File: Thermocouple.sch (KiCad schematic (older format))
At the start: 22 parts, among them P2 CONN_2, P3 CONN_3X2, U10 LMT84, U11 OPA4170, U9 MCP3901

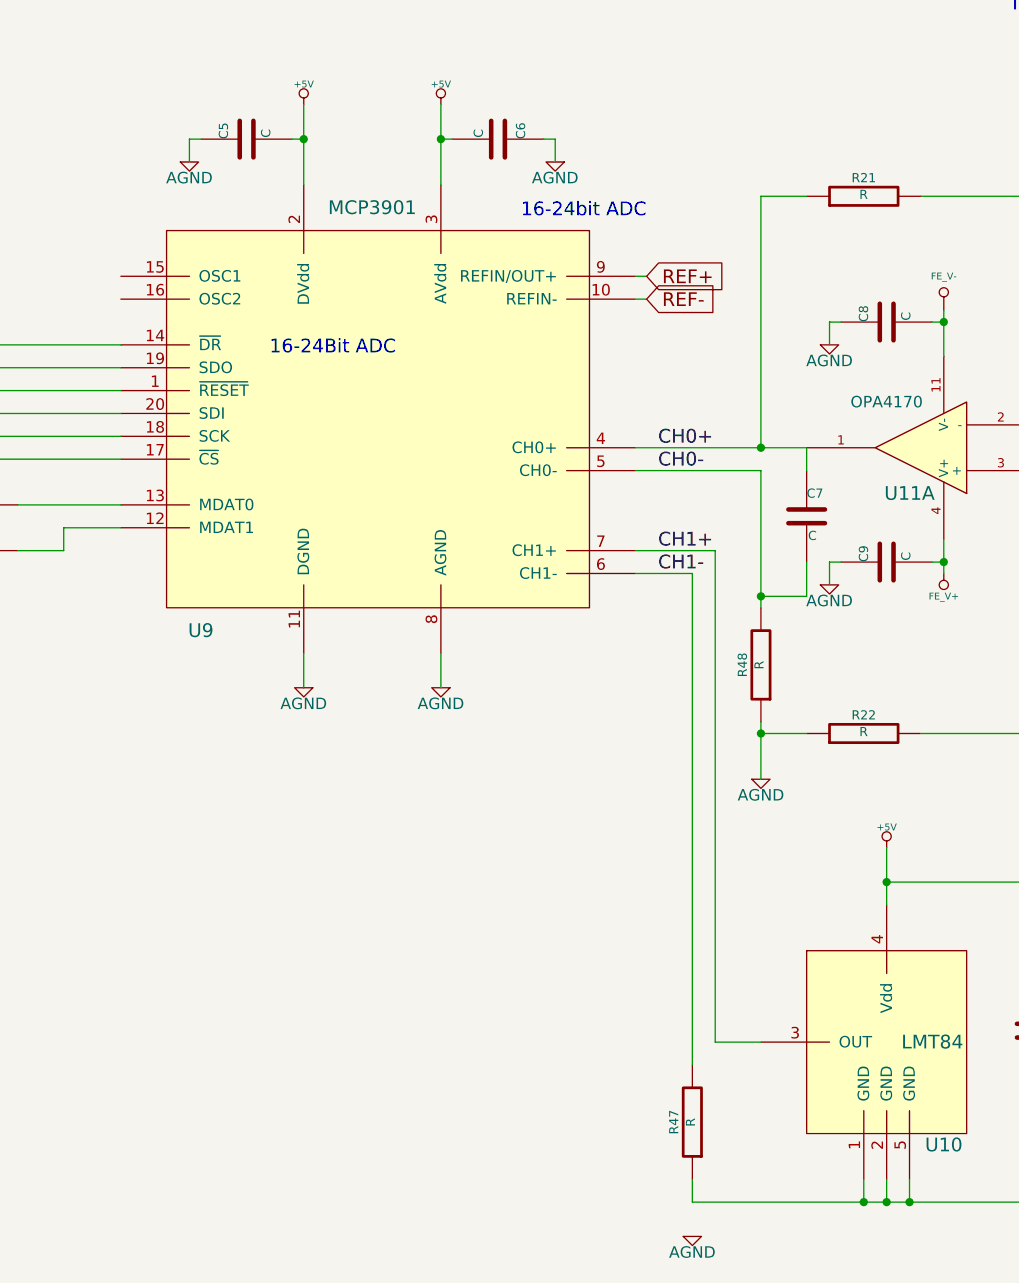
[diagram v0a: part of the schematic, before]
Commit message: Updates from Layout Work Session 4 video
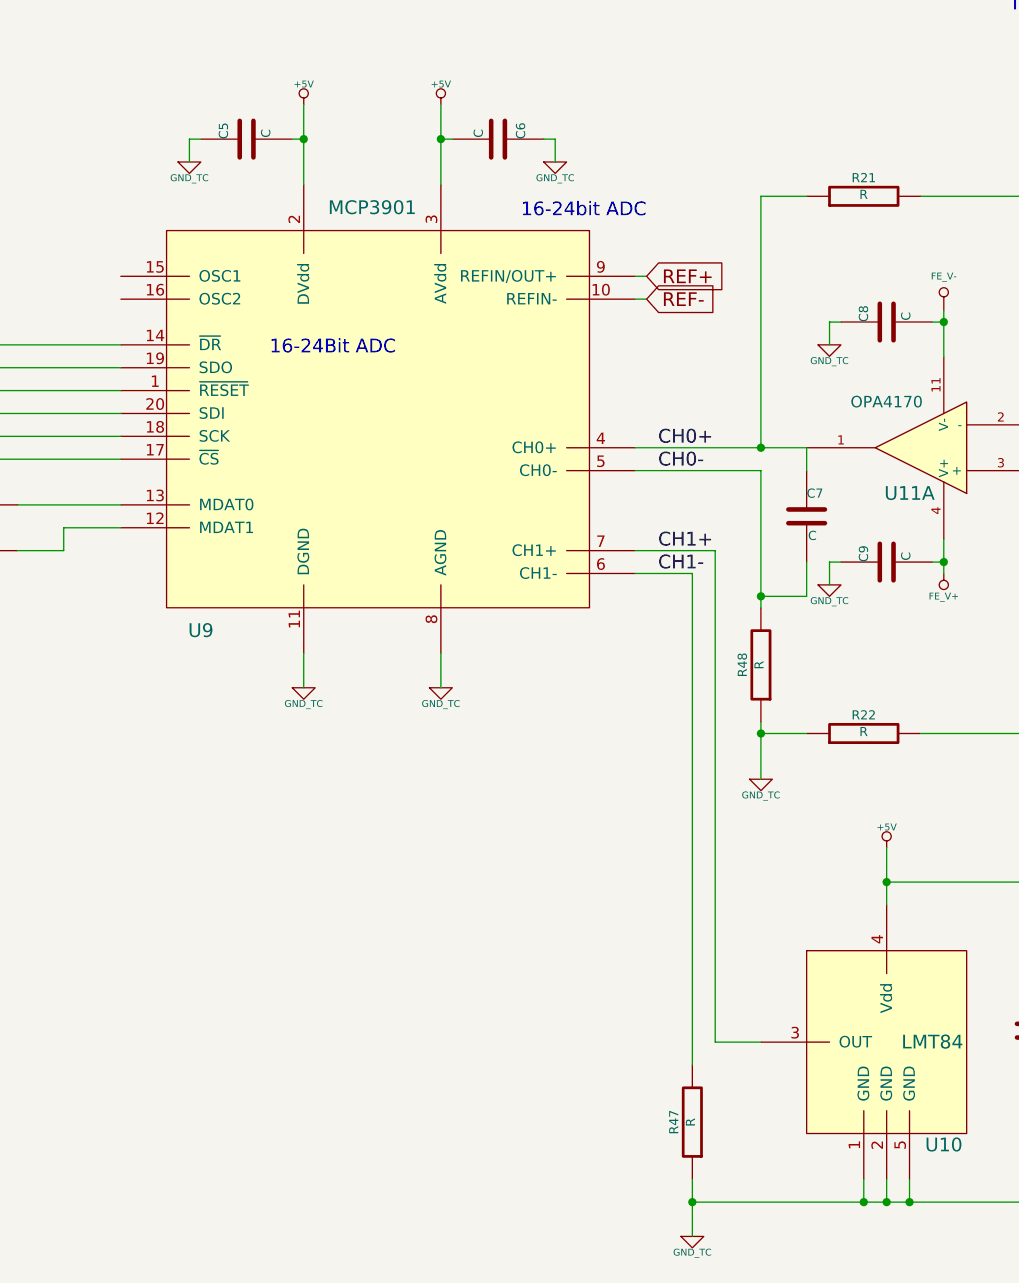
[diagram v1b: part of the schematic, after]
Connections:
- net AGND is gone; now on net GND_TC: C5.1, C6.1, C8.1, C9.1, R22.1, R48.1, U9.11 (DGND), U9.8 (AGND)
- net GND_TC: now reaches C10.2, R47.1, U10.1 (GND), U10.2 (GND), U10.5 (GND)
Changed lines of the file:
@@
 	0    -1   -1   0
-$EndComp
-$Comp
-L AGND #PWR046
-U 1 1 52F01EB3
-P 4500 4450
-F 0 "#PWR046" H 4500 4450 40  0001 C CNN
-F 1 "AGND" H 4500 4380 50  0000 C CNN
-F 2 "" H 4500 4450 60  0000 C CNN
-F 3 "" H 4500 4450 60  0000 C CNN
-	1    4500 4450
-	1    0    0    -1
 $EndComp
 Text Notes 8600 2100 0    60   ~ 0
@@
 $EndComp
 $Comp
-L AGND #PWR047
-U 1 1 53054233
-P 4200 6450
-F 0 "#PWR047" H 4200 6450 40  0001 C CNN
-F 1 "AGND" H 4200 6380 50  0000 C CNN
-F 2 "" H 4200 6450 60  0000 C CNN
-F 3 "" H 4200 6450 60  0000 C CNN
-	1    4200 6450
-	1    0    0    -1
-$EndComp
-$Comp
-L +5V #PWR048
+L +5V #PWR041
 U 1 1 530546E7
 P 5050 4750
-F 0 "#PWR048" H 5050 4840 20  0001 C CNN
+F 0 "#PWR041" H 5050 4840 20  0001 C CNN
 F 1 "+5V" H 5050 4840 30  0000 C CNN
 F 2 "" H 5050 4750 60  0000 C CNN
@@
 $EndComp
 $Comp
-L AGND #PWR049
-U 1 1 530549E4
-P 4800 2550
-F 0 "#PWR049" H 4800 2550 40  0001 C CNN
-F 1 "AGND" H 4800 2480 50  0000 C CNN
-F 2 "" H 4800 2550 60  0000 C CNN
-F 3 "" H 4800 2550 60  0000 C CNN
-	1    4800 2550
-	1    0    0    -1
-$EndComp
-$Comp
 L C C9
 U 1 1 53054A99
@@
 $EndComp
 $Comp
-L AGND #PWR050
-U 1 1 53054AA0
-P 4800 3600
-F 0 "#PWR050" H 4800 3600 40  0001 C CNN
-F 1 "AGND" H 4800 3530 50  0000 C CNN
-F 2 "" H 4800 3600 60  0000 C CNN
-F 3 "" H 4800 3600 60  0000 C CNN
-	1    4800 3600
-	1    0    0    -1
-$EndComp
-$Comp
-L +5V #PWR051
+L +5V #PWR042
 U 1 1 53054B2C
 P 3100 1500
-F 0 "#PWR051" H 3100 1590 20  0001 C CNN
+F 0 "#PWR042" H 3100 1590 20  0001 C CNN
 F 1 "+5V" H 3100 1590 30  0000 C CNN
 F 2 "" H 3100 1500 60  0000 C CNN
@@
 $EndComp
 $Comp
-L AGND #PWR052
-U 1 1 53054C58
-P 3600 1750
-F 0 "#PWR052" H 3600 1750 40  0001 C CNN
-F 1 "AGND" H 3600 1680 50  0000 C CNN
-F 2 "" H 3600 1750 60  0000 C CNN
-F 3 "" H 3600 1750 60  0000 C CNN
-	1    3600 1750
-	-1   0    0    -1
-$EndComp
-$Comp
-L AGND #PWR053
-U 1 1 5305505B
-P 3100 4050
-F 0 "#PWR053" H 3100 4050 40  0001 C CNN
-F 1 "AGND" H 3100 3980 50  0000 C CNN
-F 2 "" H 3100 4050 60  0000 C CNN
-F 3 "" H 3100 4050 60  0000 C CNN
-	1    3100 4050
-	-1   0    0    -1
-$EndComp
-$Comp
-L AGND #PWR054
-U 1 1 5305533E
-P 2500 4050
-F 0 "#PWR054" H 2500 4050 40  0001 C CNN
-F 1 "AGND" H 2500 3980 50  0000 C CNN
-F 2 "" H 2500 4050 60  0000 C CNN
-F 3 "" H 2500 4050 60  0000 C CNN
-	1    2500 4050
-	-1   0    0    -1
-$EndComp
-$Comp
-L +5V #PWR055
+L +5V #PWR043
 U 1 1 53055345
 P 2500 1500
-F 0 "#PWR055" H 2500 1590 20  0001 C CNN
+F 0 "#PWR043" H 2500 1590 20  0001 C CNN
 F 1 "+5V" H 2500 1590 30  0000 C CNN
 F 2 "" H 2500 1500 60  0000 C CNN
@@
 	0    -1   -1   0
 $EndComp
-$Comp
-L AGND #PWR056
-U 1 1 53055353
-P 2000 1750
-F 0 "#PWR056" H 2000 1750 40  0001 C CNN
-F 1 "AGND" H 2000 1680 50  0000 C CNN
-F 2 "" H 2000 1750 60  0000 C CNN
-F 3 "" H 2000 1750 60  0000 C CNN
-	1    2000 1750
-	1    0    0    -1
-$EndComp
 Text Notes 5900 5550 0    60   ~ 0
 Temperature Sensor
@@
 	4200 3550 4200 5700
 Wire Wire Line
-	4200 6300 4200 6200
+	4200 6200 4200 6450
 Connection ~ 5900 4250
 Wire Wire Line
@@
 	1050 3050 1700 3050
 $Comp
-L FE_V+ #PWR057
+L FE_V+ #PWR044
 U 1 1 530BD56D
 P 7800 4750
-F 0 "#PWR057" H 7800 4850 30  0001 C CNN
+F 0 "#PWR044" H 7800 4850 30  0001 C CNN
 F 1 "FE_V+" H 7800 4850 30  0000 C CNN
 F 2 "" H 7800 4750 60  0000 C CNN
@@
 $EndComp
 $Comp
-L FE_V+ #PWR058
+L FE_V+ #PWR045
 U 1 1 530BD573
 P 5300 3550
-F 0 "#PWR058" H 5300 3650 30  0001 C CNN
+F 0 "#PWR045" H 5300 3650 30  0001 C CNN
 F 1 "FE_V+" H 5300 3650 30  0000 C CNN
 F 2 "" H 5300 3550 60  0000 C CNN
@@
 $EndComp
 $Comp
-L FE_V+ #PWR059
+L FE_V+ #PWR046
 U 1 1 530BD635
 P 7800 1400
-F 0 "#PWR059" H 7800 1500 30  0001 C CNN
+F 0 "#PWR046" H 7800 1500 30  0001 C CNN
 F 1 "FE_V+" H 7800 1500 30  0000 C CNN
 F 2 "" H 7800 1400 60  0000 C CNN
@@
 	1    0    0    -1
 $EndComp
+$Comp
+L GND_TC #PWR047
+U 1 1 5315219A
+P 2500 4050
+F 0 "#PWR047" H 2500 4050 30  0001 C CNN
+F 1 "GND_TC" H 2500 3980 30  0000 C CNN
+F 2 "" H 2500 4050 60  0000 C CNN
+F 3 "" H 2500 4050 60  0000 C CNN
+	1    2500 4050
+	1    0    0    -1
+$EndComp
+$Comp
+L GND_TC #PWR048
+U 1 1 531521AC
+P 3100 4050
+F 0 "#PWR048" H 3100 4050 30  0001 C CNN
+F 1 "GND_TC" H 3100 3980 30  0000 C CNN
+F 2 "" H 3100 4050 60  0000 C CNN
+F 3 "" H 3100 4050 60  0000 C CNN
+	1    3100 4050
+	1    0    0    -1
+$EndComp
+$Comp
+L GND_TC #PWR049
+U 1 1 531521B7
+P 4200 6450
+F 0 "#PWR049" H 4200 6450 30  0001 C CNN
+F 1 "GND_TC" H 4200 6380 30  0000 C CNN
+F 2 "" H 4200 6450 60  0000 C CNN
+F 3 "" H 4200 6450 60  0000 C CNN
+	1    4200 6450
+	1    0    0    -1
+$EndComp
+$Comp
+L GND_TC #PWR050
+U 1 1 531521C2
+P 4500 4450
+F 0 "#PWR050" H 4500 4450 30  0001 C CNN
+F 1 "GND_TC" H 4500 4380 30  0000 C CNN
+F 2 "" H 4500 4450 60  0000 C CNN
+F 3 "" H 4500 4450 60  0000 C CNN
+	1    4500 4450
+	1    0    0    -1
+$EndComp
+$Comp
+L GND_TC #PWR051
+U 1 1 531521CD
+P 3600 1750
+F 0 "#PWR051" H 3600 1750 30  0001 C CNN
+F 1 "GND_TC" H 3600 1680 30  0000 C CNN
+F 2 "" H 3600 1750 60  0000 C CNN
+F 3 "" H 3600 1750 60  0000 C CNN
+	1    3600 1750
+	1    0    0    -1
+$EndComp
+$Comp
+L GND_TC #PWR052
+U 1 1 531521D8
+P 2000 1750
+F 0 "#PWR052" H 2000 1750 30  0001 C CNN
+F 1 "GND_TC" H 2000 1680 30  0000 C CNN
+F 2 "" H 2000 1750 60  0000 C CNN
+F 3 "" H 2000 1750 60  0000 C CNN
+	1    2000 1750
+	1    0    0    -1
+$EndComp
+Connection ~ 4200 6300
+$Comp
+L GND_TC #PWR053
+U 1 1 53152286
+P 4800 2550
+F 0 "#PWR053" H 4800 2550 30  0001 C CNN
+F 1 "GND_TC" H 4800 2480 30  0000 C CNN
+F 2 "" H 4800 2550 60  0000 C CNN
+F 3 "" H 4800 2550 60  0000 C CNN
+	1    4800 2550
+	1    0    0    -1
+$EndComp
+$Comp
+L GND_TC #PWR054
+U 1 1 53152291
+P 4800 3600
+F 0 "#PWR054" H 4800 3600 30  0001 C CNN
+F 1 "GND_TC" H 4800 3530 30  0000 C CNN
+F 2 "" H 4800 3600 60  0000 C CNN
+F 3 "" H 4800 3600 60  0000 C CNN
+	1    4800 3600
+	1    0    0    -1
+$EndComp

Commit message: Updates from Layout Work Session 5 video
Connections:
- net GND_TC: no longer C10.2, C5.1, C6.1, C8.1, C9.1, R47.1, U10.1 (GND), U10.2 (GND), U10.5 (GND), U9.11 (DGND), U9.8 (AGND)
- new net AGND: C10.2, C5.1, C6.1, C8.1, C9.1, R47.1, U10.1 (GND), U10.2 (GND), U10.5 (GND), U9.11 (DGND), U9.8 (AGND)
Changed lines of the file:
@@
 $EndComp
 $Comp
-L +5V #PWR041
+L +5V #PWR042
 U 1 1 530546E7
 P 5050 4750
-F 0 "#PWR041" H 5050 4840 20  0001 C CNN
+F 0 "#PWR042" H 5050 4840 20  0001 C CNN
 F 1 "+5V" H 5050 4840 30  0000 C CNN
 F 2 "" H 5050 4750 60  0000 C CNN
@@
 $EndComp
 $Comp
-L +5V #PWR042
+L +5V #PWR043
 U 1 1 53054B2C
 P 3100 1500
-F 0 "#PWR042" H 3100 1590 20  0001 C CNN
+F 0 "#PWR043" H 3100 1590 20  0001 C CNN
 F 1 "+5V" H 3100 1590 30  0000 C CNN
 F 2 "" H 3100 1500 60  0000 C CNN
@@
 $EndComp
 $Comp
-L +5V #PWR043
+L +5V #PWR044
 U 1 1 53055345
 P 2500 1500
-F 0 "#PWR043" H 2500 1590 20  0001 C CNN
+F 0 "#PWR044" H 2500 1590 20  0001 C CNN
 F 1 "+5V" H 2500 1590 30  0000 C CNN
 F 2 "" H 2500 1500 60  0000 C CNN
@@
 	1050 3050 1700 3050
 $Comp
-L FE_V+ #PWR044
+L FE_V+ #PWR045
 U 1 1 530BD56D
 P 7800 4750
-F 0 "#PWR044" H 7800 4850 30  0001 C CNN
+F 0 "#PWR045" H 7800 4850 30  0001 C CNN
 F 1 "FE_V+" H 7800 4850 30  0000 C CNN
 F 2 "" H 7800 4750 60  0000 C CNN
@@
 $EndComp
 $Comp
-L FE_V+ #PWR045
+L FE_V+ #PWR046
 U 1 1 530BD573
 P 5300 3550
-F 0 "#PWR045" H 5300 3650 30  0001 C CNN
+F 0 "#PWR046" H 5300 3650 30  0001 C CNN
 F 1 "FE_V+" H 5300 3650 30  0000 C CNN
 F 2 "" H 5300 3550 60  0000 C CNN
@@
 $EndComp
 $Comp
-L FE_V+ #PWR046
+L FE_V+ #PWR047
 U 1 1 530BD635
 P 7800 1400
-F 0 "#PWR046" H 7800 1500 30  0001 C CNN
+F 0 "#PWR047" H 7800 1500 30  0001 C CNN
 F 1 "FE_V+" H 7800 1500 30  0000 C CNN
 F 2 "" H 7800 1400 60  0000 C CNN
@@
 $EndComp
 $Comp
-L GND_TC #PWR047
-U 1 1 5315219A
-P 2500 4050
-F 0 "#PWR047" H 2500 4050 30  0001 C CNN
-F 1 "GND_TC" H 2500 3980 30  0000 C CNN
-F 2 "" H 2500 4050 60  0000 C CNN
-F 3 "" H 2500 4050 60  0000 C CNN
-	1    2500 4050
-	1    0    0    -1
-$EndComp
-$Comp
 L GND_TC #PWR048
-U 1 1 531521AC
-P 3100 4050
-F 0 "#PWR048" H 3100 4050 30  0001 C CNN
-F 1 "GND_TC" H 3100 3980 30  0000 C CNN
-F 2 "" H 3100 4050 60  0000 C CNN
-F 3 "" H 3100 4050 60  0000 C CNN
-	1    3100 4050
-	1    0    0    -1
-$EndComp
-$Comp
-L GND_TC #PWR049
-U 1 1 531521B7
-P 4200 6450
-F 0 "#PWR049" H 4200 6450 30  0001 C CNN
-F 1 "GND_TC" H 4200 6380 30  0000 C CNN
-F 2 "" H 4200 6450 60  0000 C CNN
-F 3 "" H 4200 6450 60  0000 C CNN
-	1    4200 6450
-	1    0    0    -1
-$EndComp
-$Comp
-L GND_TC #PWR050
 U 1 1 531521C2
 P 4500 4450
-F 0 "#PWR050" H 4500 4450 30  0001 C CNN
+F 0 "#PWR048" H 4500 4450 30  0001 C CNN
 F 1 "GND_TC" H 4500 4380 30  0000 C CNN
 F 2 "" H 4500 4450 60  0000 C CNN
@@
 	1    0    0    -1
 $EndComp
-$Comp
-L GND_TC #PWR051
-U 1 1 531521CD
+Connection ~ 4200 6300
+$Comp
+L AGND #PWR049
+U 1 1 531630FA
+P 2000 1750
+F 0 "#PWR049" H 2000 1750 40  0001 C CNN
+F 1 "AGND" H 2000 1680 50  0000 C CNN
+F 2 "" H 2000 1750 60  0000 C CNN
+F 3 "" H 2000 1750 60  0000 C CNN
+	1    2000 1750
+	1    0    0    -1
+$EndComp
+$Comp
+L AGND #PWR050
+U 1 1 53163116
 P 3600 1750
-F 0 "#PWR051" H 3600 1750 30  0001 C CNN
-F 1 "GND_TC" H 3600 1680 30  0000 C CNN
+F 0 "#PWR050" H 3600 1750 40  0001 C CNN
+F 1 "AGND" H 3600 1680 50  0000 C CNN
 F 2 "" H 3600 1750 60  0000 C CNN
 F 3 "" H 3600 1750 60  0000 C CNN
@@
 $EndComp
 $Comp
-L GND_TC #PWR052
-U 1 1 531521D8
-P 2000 1750
-F 0 "#PWR052" H 2000 1750 30  0001 C CNN
-F 1 "GND_TC" H 2000 1680 30  0000 C CNN
-F 2 "" H 2000 1750 60  0000 C CNN
-F 3 "" H 2000 1750 60  0000 C CNN
-	1    2000 1750
-	1    0    0    -1
-$EndComp
-Connection ~ 4200 6300
-$Comp
-L GND_TC #PWR053
-U 1 1 53152286
+L AGND #PWR051
+U 1 1 5316312B
+P 2500 4050
+F 0 "#PWR051" H 2500 4050 40  0001 C CNN
+F 1 "AGND" H 2500 3980 50  0000 C CNN
+F 2 "" H 2500 4050 60  0000 C CNN
+F 3 "" H 2500 4050 60  0000 C CNN
+	1    2500 4050
+	1    0    0    -1
+$EndComp
+$Comp
+L AGND #PWR052
+U 1 1 53163136
+P 3100 4050
+F 0 "#PWR052" H 3100 4050 40  0001 C CNN
+F 1 "AGND" H 3100 3980 50  0000 C CNN
+F 2 "" H 3100 4050 60  0000 C CNN
+F 3 "" H 3100 4050 60  0000 C CNN
+	1    3100 4050
+	1    0    0    -1
+$EndComp
+$Comp
+L AGND #PWR053
+U 1 1 53163155
+P 4200 6450
+F 0 "#PWR053" H 4200 6450 40  0001 C CNN
+F 1 "AGND" H 4200 6380 50  0000 C CNN
+F 2 "" H 4200 6450 60  0000 C CNN
+F 3 "" H 4200 6450 60  0000 C CNN
+	1    4200 6450
+	1    0    0    -1
+$EndComp
+$Comp
+L AGND #PWR054
+U 1 1 5316316A
 P 4800 2550
-F 0 "#PWR053" H 4800 2550 30  0001 C CNN
-F 1 "GND_TC" H 4800 2480 30  0000 C CNN
+F 0 "#PWR054" H 4800 2550 40  0001 C CNN
+F 1 "AGND" H 4800 2480 50  0000 C CNN
 F 2 "" H 4800 2550 60  0000 C CNN
 F 3 "" H 4800 2550 60  0000 C CNN
@@
 $EndComp
 $Comp
-L GND_TC #PWR054
-U 1 1 53152291
+L AGND #PWR055
+U 1 1 53163175
 P 4800 3600
-F 0 "#PWR054" H 4800 3600 30  0001 C CNN
-F 1 "GND_TC" H 4800 3530 30  0000 C CNN
+F 0 "#PWR055" H 4800 3600 40  0001 C CNN
+F 1 "AGND" H 4800 3530 50  0000 C CNN
 F 2 "" H 4800 3600 60  0000 C CNN
 F 3 "" H 4800 3600 60  0000 C CNN
